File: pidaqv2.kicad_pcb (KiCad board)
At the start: 2 copper layers, 65 x 56 mm, 5 parts, among them P1 Conn_02x20_Odd_Even

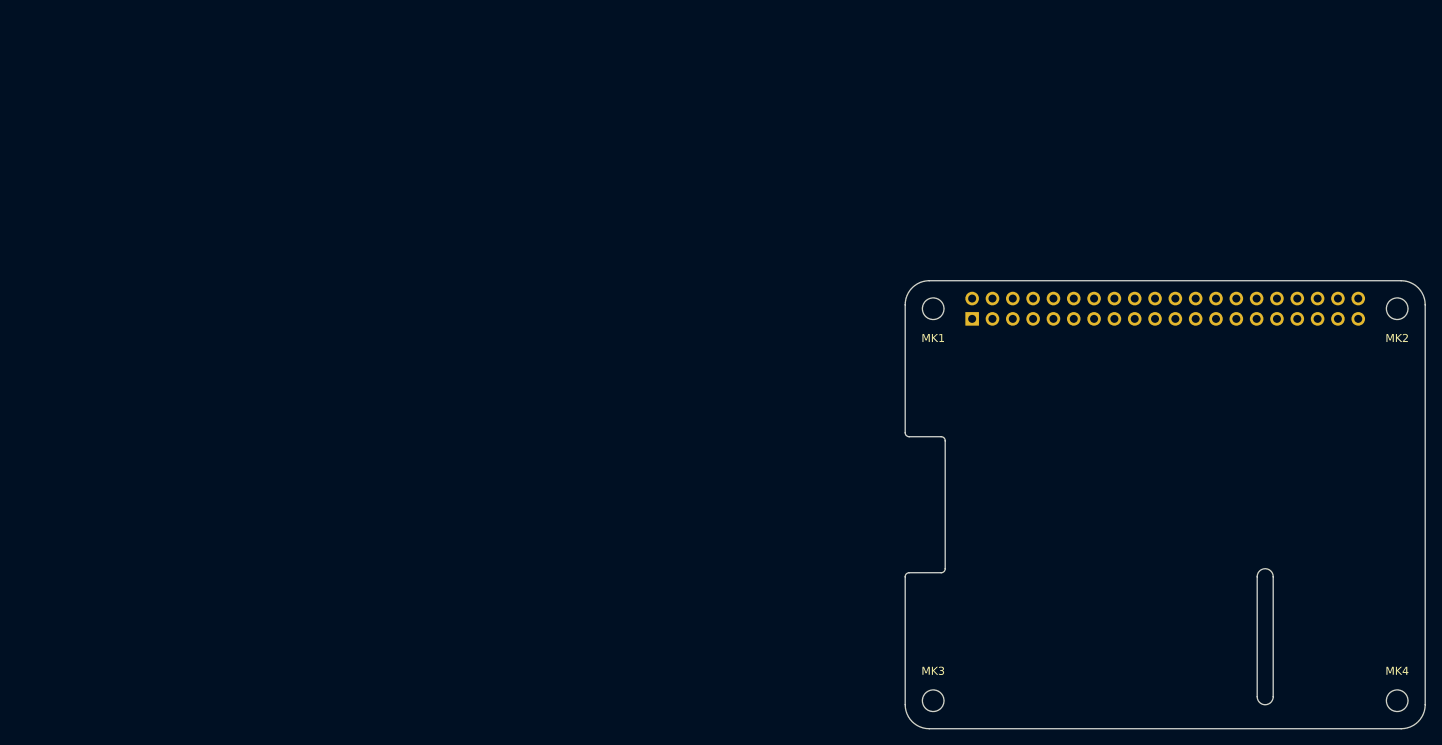
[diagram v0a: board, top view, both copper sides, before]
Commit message: added layout and online BOM viewer
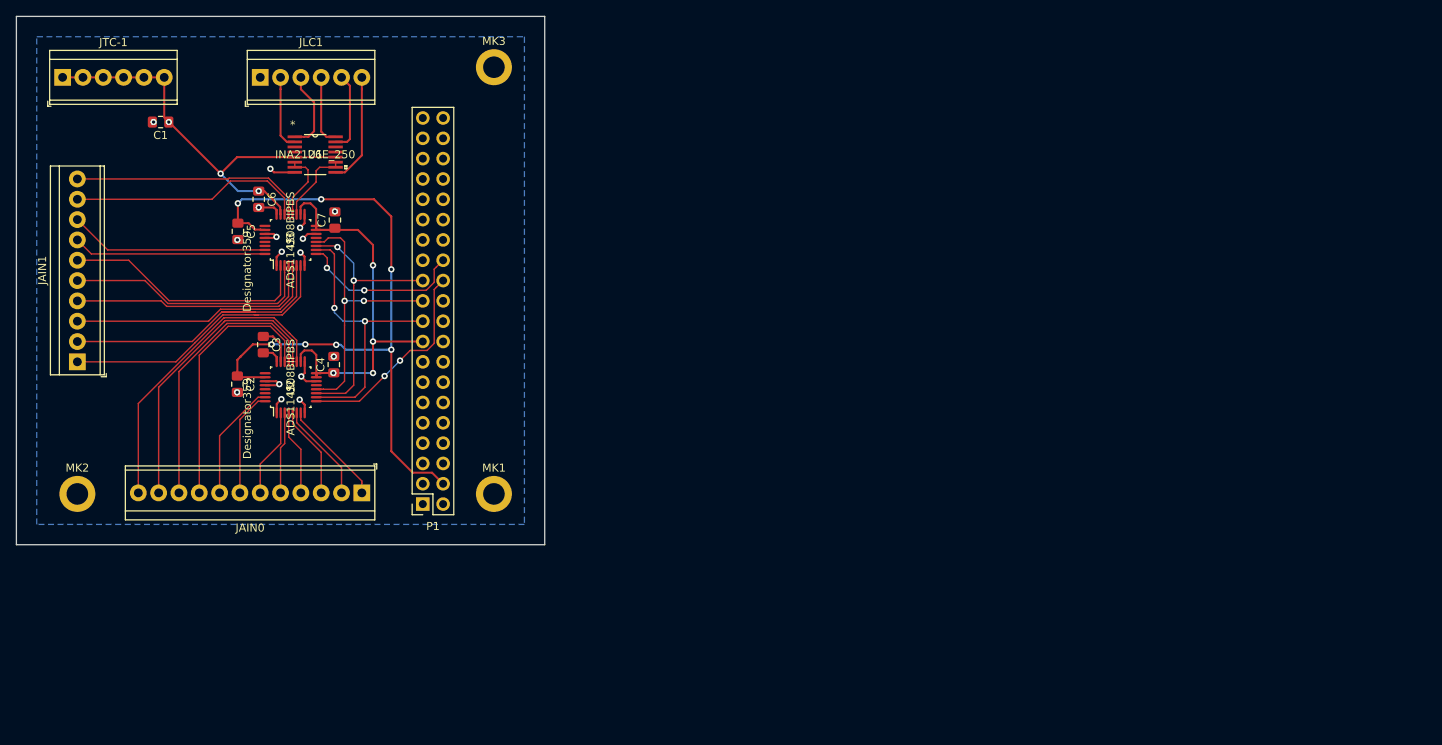
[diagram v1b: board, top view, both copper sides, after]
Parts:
- removed MK4: M2.5, MountingHole:MountingHole_2.7mm_M2.5
- added C1: 0.1uF, Capacitor_SMD:C_0805_2012Metric_Pad1.15x1.40mm_HandSolder, F.Cu at (106.9, 74.2)
- added C2: 330nF, Capacitor_SMD:C_0805_2012Metric_Pad1.15x1.40mm_HandSolder, F.Cu at (116.5, 106.9)
- added C3: 1uF, Capacitor_SMD:C_0805_2012Metric_Pad1.15x1.40mm_HandSolder, F.Cu at (119.8, 102.0)
- added C4: 0.1uF, Capacitor_SMD:C_0805_2012Metric_Pad1.15x1.40mm_HandSolder, F.Cu at (128.6, 104.5)
- added C5: 330nF, Capacitor_SMD:C_0805_2012Metric_Pad1.15x1.40mm_HandSolder, F.Cu at (116.6, 87.8)
- added C6: 1uF, Capacitor_SMD:C_0805_2012Metric_Pad1.15x1.40mm_HandSolder, F.Cu at (119.2, 83.8)
- added C7: 0.1uF, Capacitor_SMD:C_0805_2012Metric_Pad1.15x1.40mm_HandSolder, F.Cu at (128.7, 86.4)
- added JAIN0: Screw_Terminal_01x12, TerminalBlock_TE-Connectivity:TerminalBlock_TE_1-282834-2_1x12_P2.54mm_Horizontal, F.Cu at (132.1, 120.5)
- added JAIN1: Screw_Terminal_01x10, TerminalBlock_TE-Connectivity:TerminalBlock_TE_1-282834-0_1x10_P2.54mm_Horizontal, F.Cu at (96.5, 104.1)
- added JLC1: Screw_Terminal_01x06, TerminalBlock_TE-Connectivity:TerminalBlock_TE_282834-6_1x06_P2.54mm_Horizontal, F.Cu at (119.4, 68.6)
- added JTC-1: Screw_Terminal_01x06, TerminalBlock_TE-Connectivity:TerminalBlock_TE_282834-6_1x06_P2.54mm_Horizontal, F.Cu at (94.7, 68.6)
- added U1: INA2126E_250, footprints:INA2126E&slash_250, F.Cu at (126.3, 78.2)
- added U2: ADS114S08BIPBS, footprints:ADS114S08BIPBS, F.Cu at (123.2, 107.3)
- added U3: ADS114S08BIPBS, footprints:ADS114S08BIPBS, F.Cu at (123.2, 88.9)
- MK1, MK2, MK3: value M2.5 -> MountingHole_Pad; footprint MountingHole:MountingHole_2.7mm_M2.5 -> MountingHole:MountingHole_2.7mm_M2.5_ISO14580_Pad
- P1: moved to F.Cu
- moved MK2 166.6 mm to (96.5, 120.7), turned to 0 degrees
- moved MK3 96.4 mm to (148.6, 67.3)
- moved P1 72.5 mm to (139.7, 121.9), turned to 180 degrees
- moved MK1 59.6 mm to (148.6, 120.7), turned to 0 degrees
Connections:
- MK1 pad 1: (no net) -> GNDPWR
- MK2 pad 1: (no net) -> GNDPWR
- MK3 pad 1: (no net) -> GNDPWR
- P1 pad 10: /GPIO15(RXD0) -> (no net)
- P1 pad 11: /GPIO17(GEN0) -> (no net)
- P1 pad 12: /GPIO18(GEN1)(PWM0) -> (no net)
- P1 pad 13: /GPIO27(GEN2) -> (no net)
- P1 pad 15: /GPIO22(GEN3) -> (no net)
- P1 pad 16: /GPIO23(GEN4) -> (no net)
- P1 pad 18: /GPIO24(GEN5) -> (no net)
- P1 pad 19: /GPIO10(SPI0_MOSI) -> /MOSI
- P1 pad 21: /GPIO9(SPI0_MISO) -> /MISO
- P1 pad 22: /GPIO25(GEN6) -> (no net)
- P1 pad 23: /GPIO11(SPI0_SCK) -> /SCLK
- P1 pad 24: /GPIO8(SPI0_CE_N) -> /CE0
- P1 pad 26: /GPIO7(SPI1_CE_N) -> /CE1
- P1 pad 27: /ID_SD -> (no net)
- P1 pad 28: /ID_SC -> (no net)
- P1 pad 29: /GPIO5 -> (no net)
- P1 pad 3: /GPIO2(SDA1) -> (no net)
- P1 pad 31: /GPIO6 -> (no net)
- P1 pad 32: /GPIO12(PWM0) -> (no net)
- P1 pad 33: /GPIO13(PWM1) -> (no net)
- P1 pad 35: /GPIO19(SPI1_MISO) -> (no net)
- P1 pad 36: /GPIO16 -> (no net)
- P1 pad 37: /GPIO26 -> (no net)
- P1 pad 38: /GPIO20(SPI1_MOSI) -> (no net)
- P1 pad 40: /GPIO21(SPI1_SCK) -> (no net)
- P1 pad 5: /GPIO3(SCL1) -> (no net)
- P1 pad 7: /GPIO4(GCLK) -> (no net)
- P1 pad 8: /GPIO14(TXD0) -> (no net)
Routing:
- net +5V: track 0.00 -> 89.9 mm, vias 0 -> 7
- net +2.5V: track 0.00 -> 53.1 mm, vias 0 -> 3
- net +3V3: track 0.00 -> 52.7 mm, vias 0 -> 4
- net /ADC_Module/A11: track 0.00 -> 39.3 mm
- net /sheet5F3BC562/A1: track 0.00 -> 38.4 mm
- net /ADC_Module/A10: track 0.00 -> 37.1 mm
- net /MOSI: track 0.00 -> 36.1 mm, vias 0 -> 2
- net /sheet5F3BC562/A0: track 0.00 -> 35.6 mm
- net /MISO: track 0.00 -> 35.1 mm, vias 0 -> 2
- net /ADC_Module/A9: track 0.00 -> 34.9 mm
- net /SCLK: track 0.00 -> 34.6 mm, vias 0 -> 2
- net /ADC_Module/A8: track 0.00 -> 32.8 mm
- net /sheet5F3BC562/A2: track 0.00 -> 32.1 mm
- net /sheet5F3BC562/A5: track 0.00 -> 31.5 mm
- net /sheet5F3BC562/A4: track 0.00 -> 31.3 mm
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- added copper zone on B.Cu, net GND
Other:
- board size 65 x 56 mm -> 66 x 66 mm
- net class Default: clearance 0.2 -> 0.1778; trace_width 0.2 -> 0.1778; via_dia 0.9 -> 0.8; via_drill 0.6 -> 0.4
- net class Power removed
- rule pad_to_mask_clearance: 0 -> 0.051
- rule trace_clearance: 0.2 -> 0.1778
- rule trace_min: 0.1524 -> 0.1778
- rule via_min_drill: 0.5 -> 0.3
- rule via_min_size: 0.8 -> 0.4
- board text removed: "CAMERA"
- board text removed: "DISPLAY"
- board text removed: "RASPBERRY-PI 40-PIN ADDON BOARD VIEW FROM TOP NOTE: P1 SHOULD BE FITTED ON THE REVERSE OF THE BOARD ADD EDGE CUTS FROM CAMERA AND DISPLAY PORTS AS REQUIRED"
- board text removed: "RJ45"
- board text removed: "USB"
